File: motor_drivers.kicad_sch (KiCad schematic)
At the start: 23 parts, among them U7 AMS1117-3.3, U8 TB6612FNG, U9 TB6612FNG

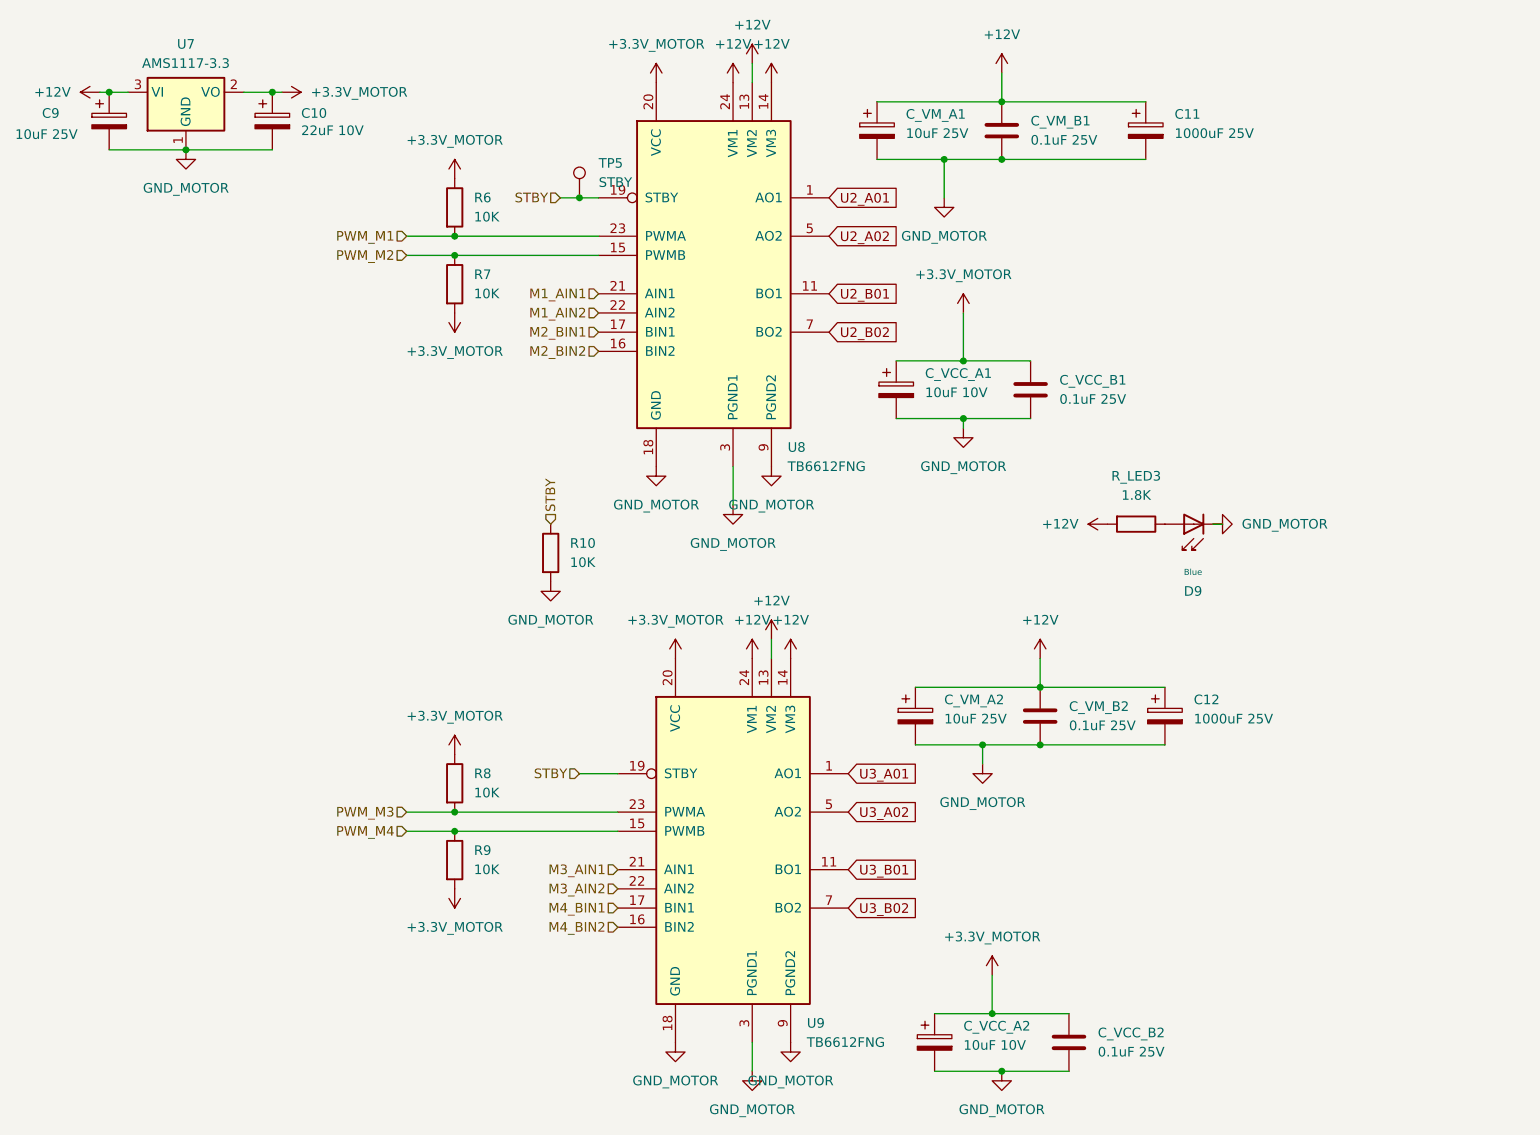
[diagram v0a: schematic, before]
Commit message: Updating routing with new terminal block
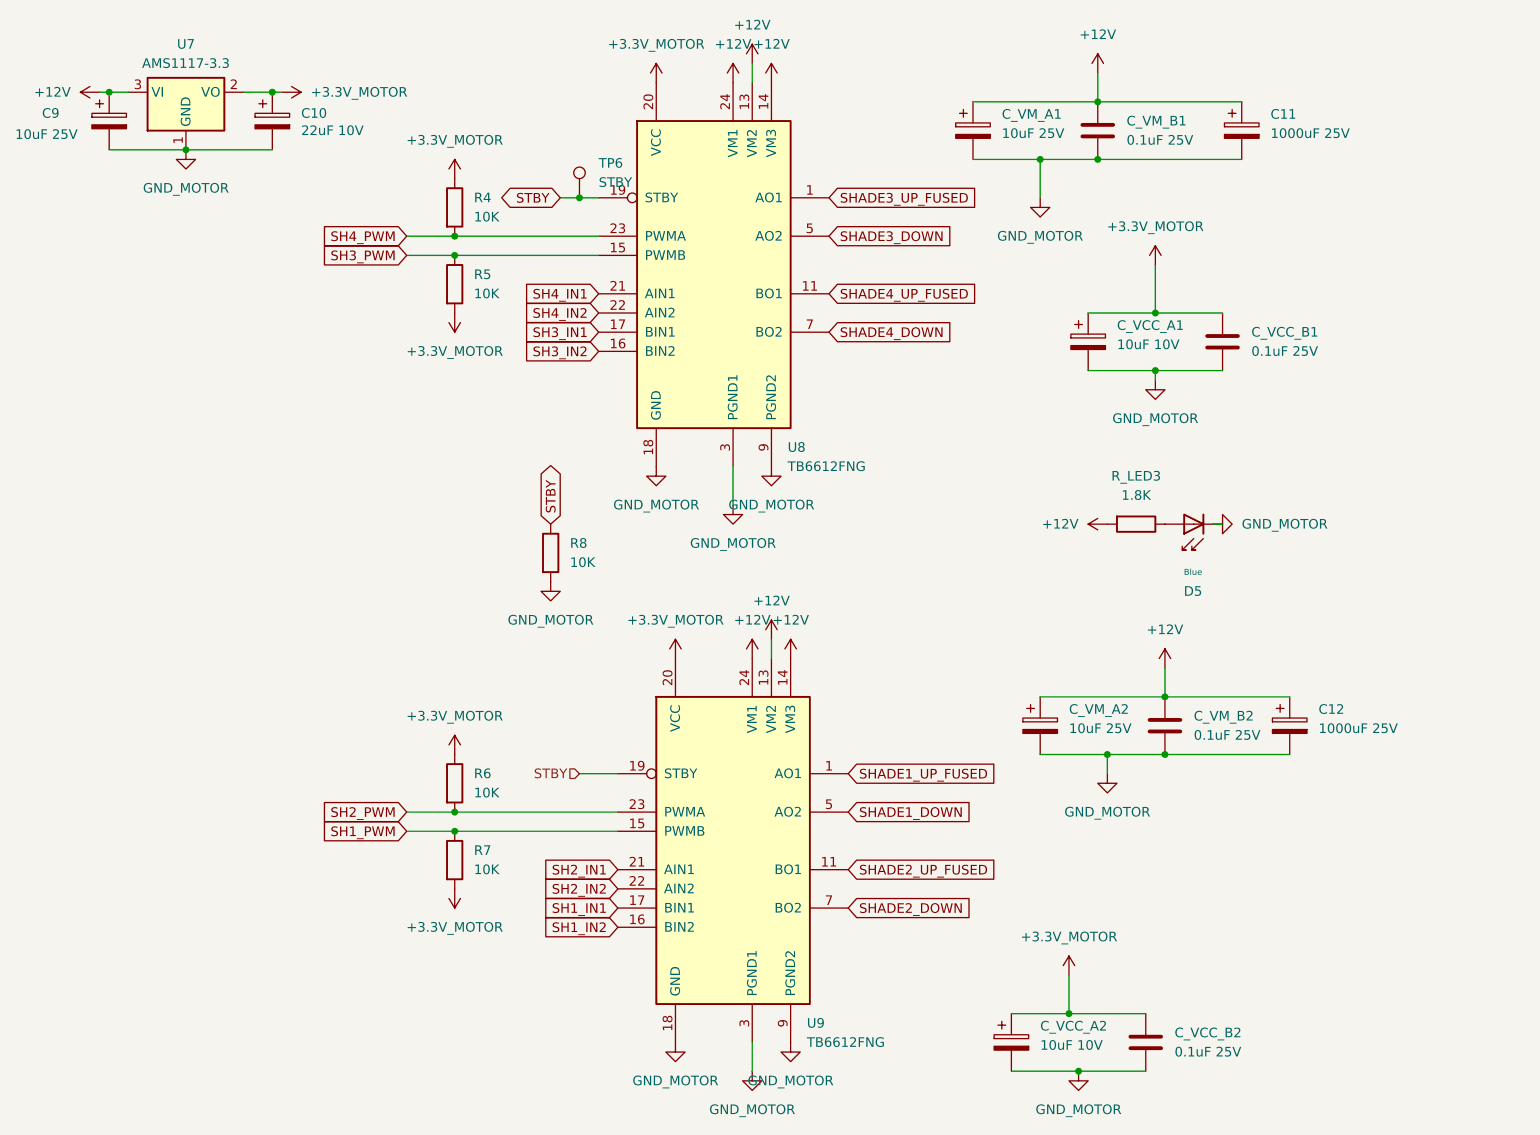
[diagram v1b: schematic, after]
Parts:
- TP6: renamed from TP5; footprint barn_shade_controller:TestPoint_Pad_D1.0mm_No_SolderMask -> TestPoint:TestPoint_Pad_D1.0mm
- renumbered D9 to D5, R6 to R4, R7 to R5, R8 to R6, R9 to R7, R10 to R8
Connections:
- net M1_AIN1 renamed SH4_IN1
- net M1_AIN2 renamed SH4_IN2
- net M2_BIN1 renamed SH3_IN1
- net M2_BIN2 renamed SH3_IN2
- net M3_AIN1 renamed SH2_IN1
- net M3_AIN2 renamed SH2_IN2
- net M4_BIN1 renamed SH1_IN1
- net M4_BIN2 renamed SH1_IN2
- net PWM_M1 renamed SH4_PWM
- net PWM_M2 renamed SH3_PWM
- net PWM_M3 renamed SH2_PWM
- net PWM_M4 renamed SH1_PWM
- net U2_A01 renamed SHADE3_UP_FUSED
- net U2_A02 renamed SHADE3_DOWN
- net U2_B01 renamed SHADE4_UP_FUSED
- net U2_B02 renamed SHADE4_DOWN
- net U3_A01 renamed SHADE1_UP_FUSED
- net U3_A02 renamed SHADE1_DOWN
- net U3_B01 renamed SHADE2_UP_FUSED
- net U3_B02 renamed SHADE2_DOWN
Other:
- moved on the sheet: C11, C12, C_VCC_A1, C_VCC_A2, C_VCC_B1, C_VCC_B2, C_VM_A1, C_VM_A2, C_VM_B1, C_VM_B2

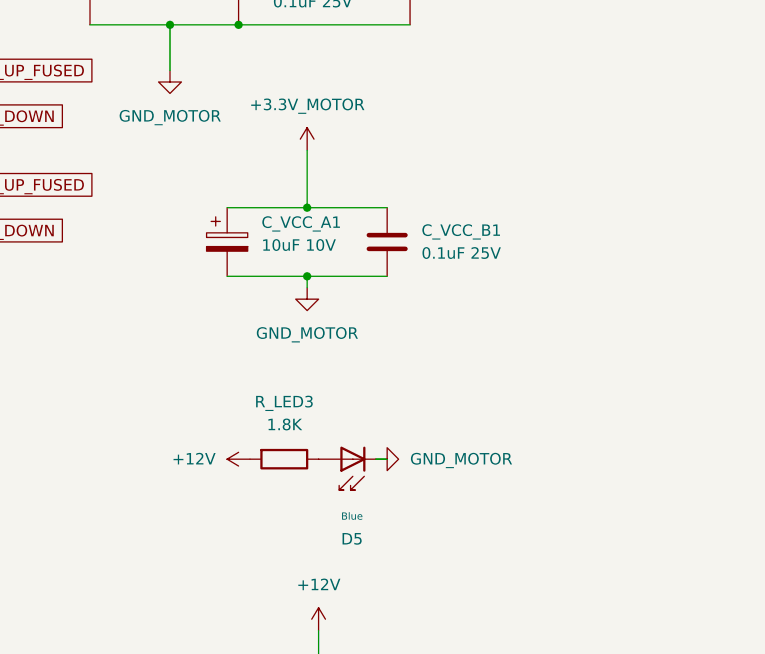
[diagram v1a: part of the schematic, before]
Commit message: Added RTS/DTS programing via UART circuitry, added LED control circuitry.
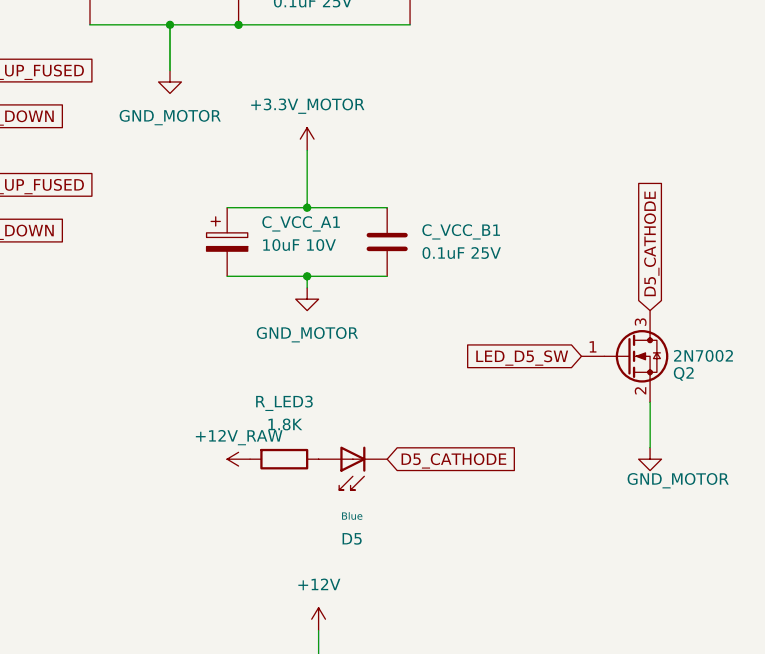
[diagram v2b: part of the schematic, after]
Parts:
- added Q2: 2N7002, Package_TO_SOT_SMD:SOT-23, symbol Transistor_FET:2N7002
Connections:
- net +12V: no longer R_LED3.2
- net GND_MOTOR: now also Q2.2 (S); no longer D5.1
- new net +12V_RAW: R_LED3.2
- new net D5_CATHODE: D5.1, Q2.3 (D)
- new net LED_D5_SW: Q2.1 (G)
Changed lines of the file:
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@@
-	(wire
-		(pts
-			(xy 171.45 81.28) (xy 170.18 81.28)
-		)
-		(stroke
-			(width 0)
-			(type default)
-		)
-	)
 	(wire
 		(pts
@@
 		(pts
 			(xy 156.21 111.76) (xy 156.21 114.3)
+		)
+		(stroke
+			(width 0)
+			(type default)
+		)
+	)
+	(wire
+		(pts
+			(xy 200.66 74.93) (xy 200.66 80.01)
 		)
 		(stroke
@@
 		)
 	)
+	(global_label "D5_CATHODE"
+		(shape input)
+		(at 200.66 64.77 90)
+		(fields_autoplaced yes)
+		(effects
+			(font
+				(size 1.27 1.27)
+			)
+			(justify left)
+		)
+		(property "Intersheetrefs" "${INTERSHEET_REFS}"
+			(at 210.9218 64.77 0)
+			(hide yes)
+			(show_name no)
+			(do_not_autoplace no)
+			(effects
+				(font
+					(size 1.27 1.27)
+				)
+				(justify left)
+			)
+		)
+	)
 	(global_label "SH3_PWM"
 		(shape input)
@@
 		)
 	)
+	(global_label "D5_CATHODE"
+		(shape input)
+		(at 171.45 81.28 0)
+		(fields_autoplaced yes)
+		(effects
+			(font
+				(size 1.27 1.27)
+			)
+			(justify left)
+		)
+		(property "Intersheetrefs" "${INTERSHEET_REFS}"
+			(at 181.6018 81.28 0)
+			(hide yes)
+			(show_name no)
+			(do_not_autoplace no)
+			(effects
+				(font
+					(size 1.27 1.27)
+				)
+				(justify left)
+			)
+		)
+	)
 	(global_label "STBY"
 		(shape bidirectional)
@@
 		(property "Intersheetrefs" "${INTERSHEET_REFS}"
 			(at 140.2056 50.8 0)
+			(hide yes)
+			(show_name no)
+			(do_not_autoplace no)
+			(effects
+				(font
+					(size 1.27 1.27)
+				)
+				(justify left)
+			)
+		)
+	)
+	(global_label "LED_D5_SW"
+		(shape input)
+		(at 193.04 69.85 180)
+		(fields_autoplaced yes)
+		(effects
+			(font
+				(size 1.27 1.27)
+			)
+			(justify right)
+		)
+		(property "Intersheetrefs" "${INTERSHEET_REFS}"
+			(at 182.9582 69.85 0)
 			(hide yes)
 			(show_name no)
@@
 	)
 	(symbol
+		(lib_id "power:GND")
+		(at 200.66 80.01 0)
+		(unit 1)
+		(body_style 1)
+		(exclude_from_sim no)
+		(in_bom yes)
+		(on_board yes)
+		(in_pos_files yes)
+		(dnp no)
+		(fields_autoplaced yes)
+		(property "Reference" "#PWR0121"
+			(at 200.66 84.29 0)
+			(hide yes)
+			(show_name no)
+			(do_not_autoplace no)
+			(effects
+				(font
+					(size 1.27 1.27)
+				)
+			)
+		)
+		(property "Value" "GND_MOTOR"
+			(at 203.7577 83.5279 0)
+			(show_name no)
+			(do_not_autoplace no)
+			(effects
+				(font
+					(size 1.27 1.27)
+				)
+			)
+		)
+		(property "Footprint" ""
+			(at 200.66 80.01 0)
+			(hide yes)
+			(show_name no)
+			(do_not_autoplace no)
+			(effects
+				(font
+					(size 1.27 1.27)
+				)
+			)
+		)
+		(property "Datasheet" ""
+			(at 200.66 80.01 0)
+			(hide yes)
+			(show_name no)
+			(do_not_autoplace no)
+			(effects
+				(font
+					(size 1.27 1.27)
+				)
+			)
+		)
+		(property "Description" "Power symbol creates a global label with name \"GND\" , ground"
+			(at 200.66 80.01 0)
+			(hide yes)
+			(show_name no)
+			(do_not_autoplace no)
+			(effects
+				(font
+					(size 1.27 1.27)
+				)
+			)
+		)
+		(pin "1"
+		)
+		(instances
+			(project "barn-blinds-controller"
+				(path "/aa90962a-81b9-423d-8acd-c4e83fa798bb/46d07447-40e9-4479-b54c-a052829b7861"
+					(reference "#PWR0121")
+					(unit 1)
+				)
+			)
+		)
+	)
+	(symbol
 		(lib_id "power:+12V")
 		(at 109.22 20.32 0)
@@
 	)
 	(symbol
+		(lib_id "Transistor_FET:2N7002")
+		(at 198.12 69.85 0)
+		(unit 1)
+		(body_style 1)
+		(exclude_from_sim no)
+		(in_bom yes)
+		(on_board yes)
+		(in_pos_files yes)
+		(dnp no)
+		(fields_autoplaced yes)
+		(property "Reference" "Q2"
+			(at 203.2 71.755 0)
+			(show_name no)
+			(do_not_autoplace no)
+			(effects
+				(font
+					(size 1.27 1.27)
+				)
+				(justify left)
+			)
+		)
+		(property "Value" "2N7002"
+			(at 203.2 69.85 0)
+			(show_name no)
+			(do_not_autoplace no)
+			(effects
+				(font
+					(size 1.27 1.27)
+				)
+				(justify left)
+			)
+		)
+		(property "Footprint" "Package_TO_SOT_SMD:SOT-23"
+			(at 203.2 67.945 0)
+			(hide yes)
+			(show_name no)
+			(do_not_autoplace no)
+			(effects
+				(font
+					(size 1.27 1.27)
+					(italic yes)
+				)
+				(justify left)
+			)
+		)
+		(property "Datasheet" "https://www.onsemi.com/pub/Collateral/NDS7002A-D.PDF"
+			(at 198.12 69.85 0)
+			(hide yes)
+			(show_name no)
+			(do_not_autoplace no)
+			(effects
+				(font
+					(size 1.27 1.27)
+				)
+			)
+		)
+		(property "Description" "0.115A Id, 60V Vds, N-Channel MOSFET, SOT-23"
+			(at 198.12 69.85 0)
+			(hide yes)
+			(show_name no)
+			(do_not_autoplace no)
+			(effects
+				(font
+					(size 1.27 1.27)
+				)
+			)
+		)
+		(pin "1"
+		)
+		(pin "2"
+		)
+		(pin "3"
+		)
+		(instances
+			(project "barn-blinds-controller"
+				(path "/aa90962a-81b9-423d-8acd-c4e83fa798bb/46d07447-40e9-4479-b54c-a052829b7861"
+					(reference "Q2")
+					(unit 1)
+				)
+			)
+		)
+	)
+	(symbol
 		(lib_id "power:+12V")
 		(at 154.94 21.59 0)
@@
 			)
 		)
-		(property "Value" "+12V"
-			(at 152.4 81.2799 90)
-			(show_name no)
-			(do_not_autoplace no)
-			(effects
-				(font
-					(size 1.27 1.27)
-				)
-				(justify left)
+		(property "Value" "+12V_RAW"
+			(at 154.94 78.74 90)
+			(show_name no)
+			(do_not_autoplace no)
+			(effects
+				(font
+					(size 1.27 1.27)
+				)
 			)
 		)
@@
 					(unit 1)
 				)
-			)
-		)
-	)
-	(symbol
-		(lib_id "power:GND")
-		(at 170.18 81.28 90)
-		(unit 1)
-		(body_style 1)
-		(exclude_from_sim no)
-		(in_bom yes)
-		(on_board yes)
-		(in_pos_files yes)
-		(dnp no)
-		(fields_autoplaced yes)
-		(property "Reference" "#PWR079"
-			(at 176.53 81.28 0)
-			(hide yes)
-			(show_name no)
-			(do_not_autoplace no)
-			(effects
-				(font
-					(size 1.27 1.27)
-				)
-			)
-		)
-		(property "Value" "GND_MOTOR"
-			(at 173.99 81.2799 90)
-			(show_name no)
-			(do_not_autoplace no)
-			(effects
-				(font
-					(size 1.27 1.27)
-				)
-				(justify right)
-			)
-		)
-		(property "Footprint" ""
-			(at 170.18 81.28 0)
-			(hide yes)
-			(show_name no)
-			(do_not_autoplace no)
-			(effects
-				(font
-					(size 1.27 1.27)
-				)
-			)
-		)
-		(property "Datasheet" ""
-			(at 170.18 81.28 0)
-			(hide yes)
-			(show_name no)
-			(do_not_autoplace no)
-			(effects
-				(font
-					(size 1.27 1.27)
-				)
-			)
-		)
-		(property "Description" "Power symbol creates a global label with name \"GND\" , ground"
-			(at 170.18 81.28 0)
-			(hide yes)
-			(show_name no)
-			(do_not_autoplace no)
-			(effects
-				(font
-					(size 1.27 1.27)
-				)
-			)
-		)
-		(pin "1"
-		)
-		(instances
-			(project "barn-blinds-controller"
-				(path "/aa90962a-81b9-423d-8acd-c4e83fa798bb/46d07447-40e9-4479-b54c-a052829b7861"
-					(reference "#PWR079")
-					(unit 1)
-				)
